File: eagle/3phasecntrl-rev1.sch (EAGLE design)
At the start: 71 parts, among them IC3 ATXmega32A4U, IC4 LD1117S50, IC6 LD1117S33, T1 BC847, T2 BC847, U1 LM5008MM

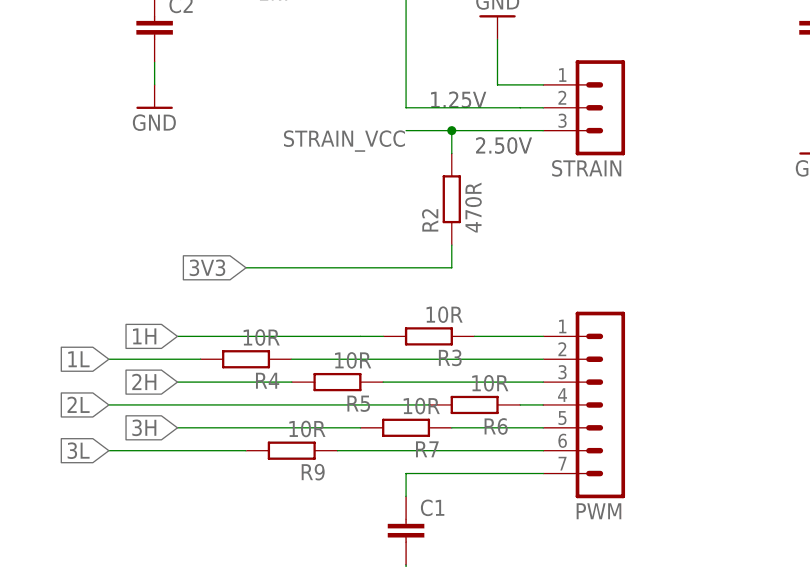
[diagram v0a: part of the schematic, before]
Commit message: Strain sensor with signed ad value, highest gain. Averaging moved, produced aliasing issues. Bootloader dind;t want to stay in bootload mode. Removed hex files from commit. Bom added
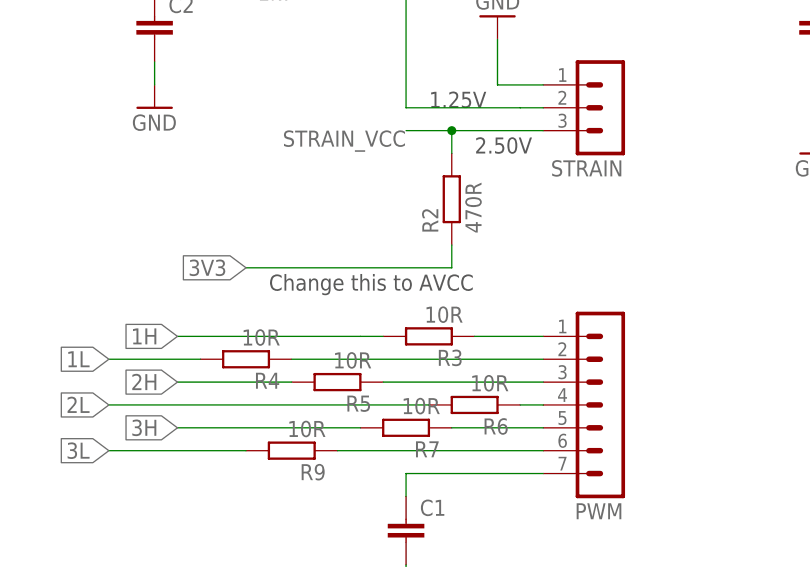
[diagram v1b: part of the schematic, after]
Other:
- note added: "Change this to AVCC"
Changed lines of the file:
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@@
 <text x="345.44" y="236.22" size="1.778" layer="97">100k = 12V DATA BUS</text>
 <text x="345.44" y="231.14" size="1.778" layer="97">47k = 24V DATA BUS</text>
+<text x="243.84" y="40.64" size="1.778" layer="97">Change this to AVCC</text>
 </plain>
 <instances>
